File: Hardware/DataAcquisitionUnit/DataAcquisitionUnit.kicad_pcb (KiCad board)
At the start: 2 copper layers, 85 x 60 mm, 64 parts, among them J1 Conn_Coaxial, J10 DE9_Pins_MountingHoles, J11 DE9_Pins_MountingHoles, J2 Conn_Coaxial, J3 Conn_Coaxial, J4 Conn_Coaxial, J9 DE9_Pins_MountingHoles, U1 LM2901, U2 LD1117S50TR_SOT223

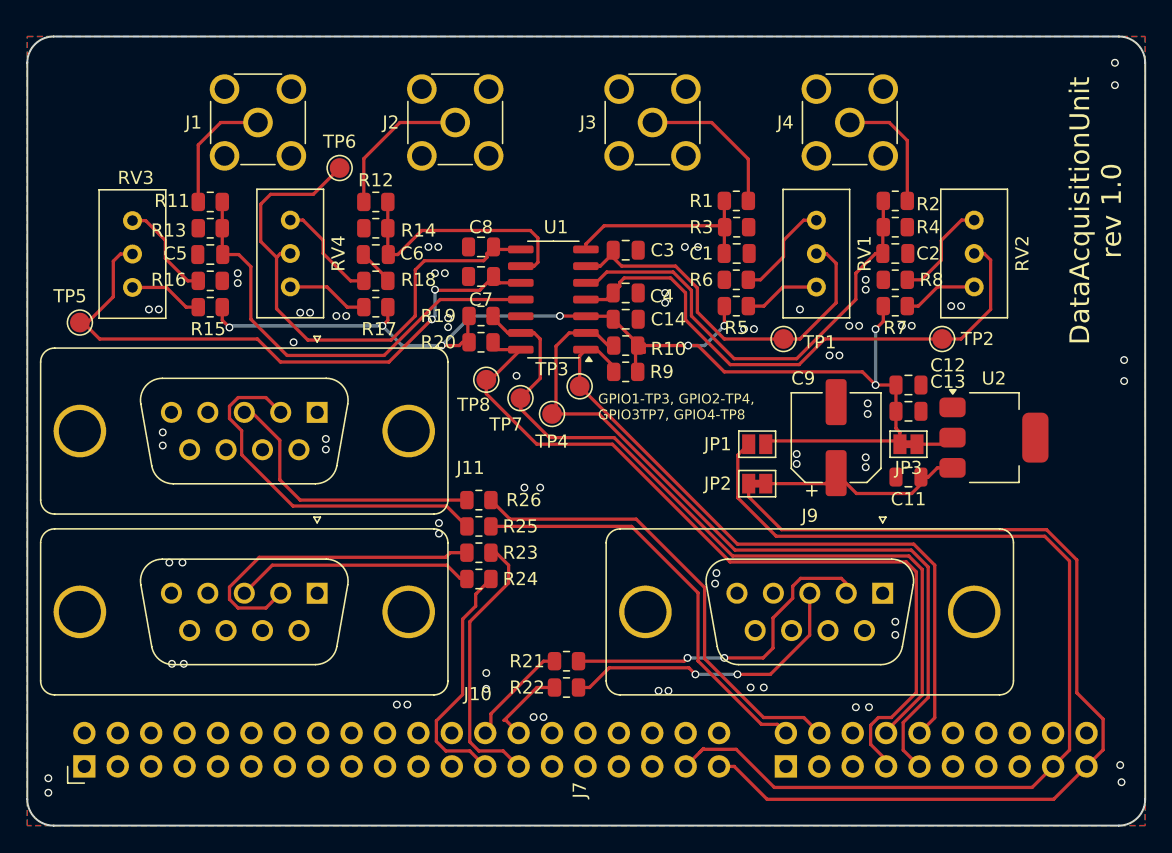
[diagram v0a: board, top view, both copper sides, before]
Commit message: make boards smaller, fix sd card slot
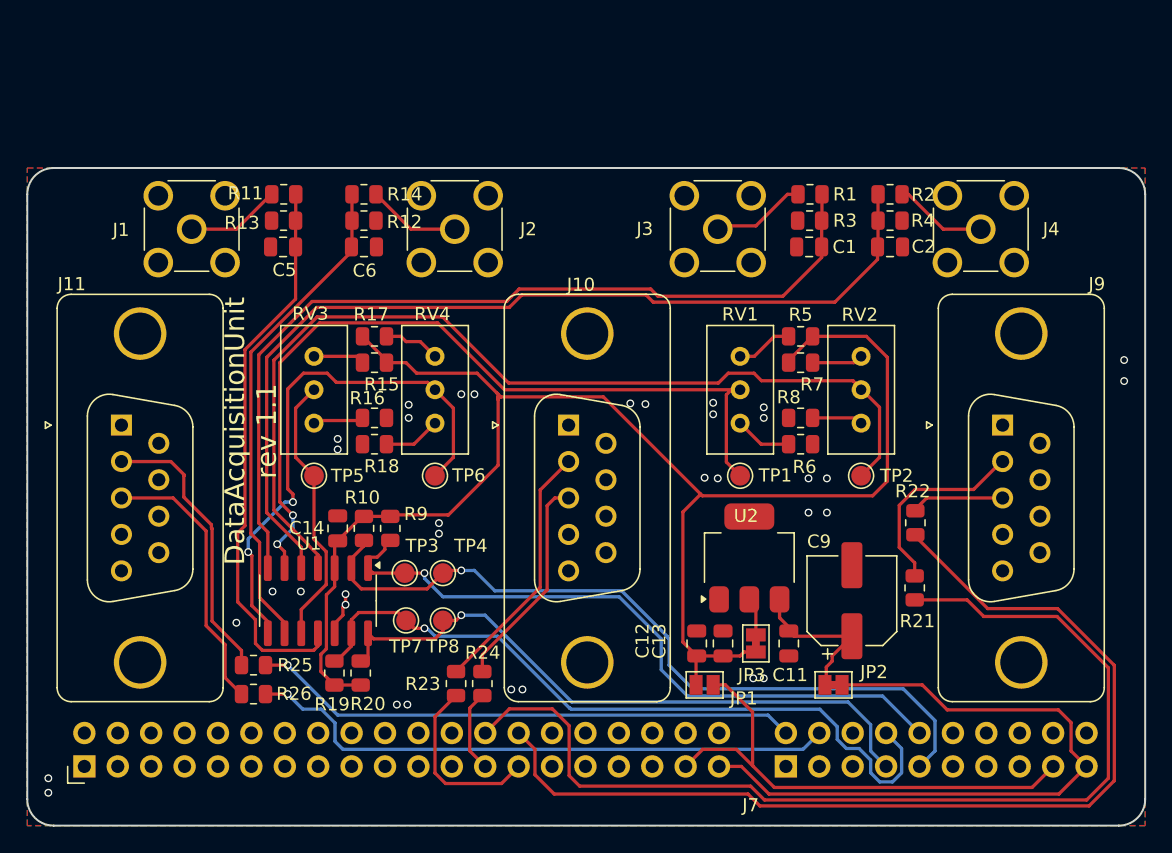
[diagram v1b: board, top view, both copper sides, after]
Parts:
- removed C3, C4, C7, C8: 3n3, Capacitor_SMD:C_0805_2012Metric
- moved R19 29.4 mm to (153.3, 108.4), turned to -90 degrees
- moved R22 29.3 mm to (197.5, 97.0), turned to 90 degrees
- moved U1 29.1 mm to (152.1, 102.9), turned to -90 degrees
- moved C14 27.1 mm to (153.6, 97.4), turned to 90 degrees
- moved R21 27.1 mm to (197.5, 101.9), turned to 90 degrees
- moved R20 26.8 mm to (155.3, 108.4), turned to -90 degrees
- moved C12 25.4 mm to (180.9, 106.2), turned to 90 degrees
- moved TP6 24.5 mm to (161.0, 93.4)
- moved R10 24.3 mm to (155.6, 97.4), turned to 90 degrees
- moved J10 23.0 mm to (171.2, 89.5), turned to 90 degrees
- moved R26 22.6 mm to (147.2, 110.0)
- moved C13 22.6 mm to (182.9, 106.2), turned to 90 degrees
- moved R9 21.5 mm to (157.6, 97.4), turned to 90 degrees
- moved TP5 21.3 mm to (151.8, 93.4)
- moved U2 20.7 mm to (184.9, 99.7), turned to 90 degrees
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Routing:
- net USART1_RX: track 7.52 -> 79.2 mm
- net USART1_TX: track 6.38 -> 77.5 mm
- net Net-(U1B-+): track 15.4 -> 67.6 mm
- net 3V3_FROM_MAINBOARD: track 78.5 -> 38.3 mm
- net Net-(U1A-+): track 34.5 -> 72.0 mm
- net Net-(U1B--): track 29.0 -> 62.9 mm, vias 0 -> 2
- net Net-(U1A--): track 42.5 -> 73.9 mm
- net 3V3: track 90.1 -> 117.6 mm, vias 8 -> 0
- net Net-(U1C--): track 45.8 -> 20.8 mm, vias 2 -> 0
- net 5V: track 75.0 -> 52.1 mm
- net Net-(U1D-+): track 19.6 -> 36.3 mm
- net Net-(J9-Pad3): track 23.3 -> 6.99 mm, vias 2 -> 0
- net GPIO_22: track 61.7 -> 49.0 mm, vias 0 -> 1
- net USART2_TX: track 18.6 -> 6.27 mm
- net Net-(J9-Pad2): track 25.0 -> 15.0 mm, vias 2 -> 0
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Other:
- board size 85 x 60 mm -> 85 x 50 mm
- board text added: "206,15-172.5=33,65"
- board text added: "DataAcquisitionUnit rev 1.1"
- board text added: "x=172,5"
- board text removed: "DataAcquisitionUnit rev 1.0"

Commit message: make hw
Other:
- board text added: "GPIO1-TP3, GPIO2-TP4, GPIO3-TP7, GPIO4-TP8"
- board text removed: "GPIO1-TP3, GPIO2-TP4, GPIO3TP7, GPIO4-TP8"
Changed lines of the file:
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@@
 		(tags "test point SMD pad")
 		(property "Reference" "TP3"
-			(at 2.075 1.325 180)
+			(at 1.8 1.3 180)
 			(layer "F.SilkS")
 			(effects
@@
 		(tags "test point SMD pad")
 		(property "Reference" "TP8"
-			(at -1.975 0 180)
+			(at 0.2 3 180)
 			(layer "F.SilkS")
 			(effects
@@
 		(tags "test point SMD pad")
 		(property "Reference" "TP4"
-			(at 2.075 2.125 180)
+			(at 0 2.8 180)
 			(layer "F.SilkS")
 			(effects
@@
 		)
 	)
-	(gr_text "GPIO1-TP3, GPIO2-TP4, \nGPIO3TP7, GPIO4-TP8"
-		(at 163.85 98.4 -0)
+	(gr_text "GPIO1-TP3, GPIO2-TP4, \nGPIO3-TP7, GPIO4-TP8"
+		(at 163.85 98.4 0)
 		(layer "B.SilkS")
 		(effects
